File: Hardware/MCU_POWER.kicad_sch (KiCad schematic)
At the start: 28 parts, among them J4 USB_B, U1 HPM5E31IGN1, X1 24M,10ppm

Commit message: 调整引脚，拉线
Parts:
- J4: footprint Connector_USB:USB_B_OST_USB-B1HSxx_Horizontal -> Library:USB_B_OST_USB-B1HSxx_Horizontal
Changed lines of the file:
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@@
 			)
 		)
-		(property "Footprint" "Connector_USB:USB_B_OST_USB-B1HSxx_Horizontal"
+		(property "Footprint" "Library:USB_B_OST_USB-B1HSxx_Horizontal"
 			(at 146.05 172.72 0)
 			(effects
@@
 			(at 142.24 171.45 0)
 			(effects
+				(font
+					(size 1.27 1.27)
+				)
+				(hide yes)
+			)
+		)
+		(property "立创编号" ""
+			(at 142.24 171.45 0)
+			(effects
+				(font
+					(size 1.27 1.27)
+				)
+				(hide yes)
+			)
+		)
+		(property "华秋编号" ""
+			(at 142.24 171.45 0)
+			(effects

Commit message: 拉线
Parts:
- added R132, R133: 10K,1%, Resistor_SMD:R_0402_1005Metric, symbol HPM6280Foc:0402WGF1002TCE
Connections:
- net +3.3V: now also U1.M2 (DCDC_IN); no longer U1.N4 (VPMC), U1.P4 (VPMC)
- net GND: now also R132.1, R133.1; no longer U1.A1 (VSS), U1.A14 (VSS), U1.E10 (VSS), U1.E5 (VSS), U1.F7 (VSS), U1.F8 (VSS), U1.G7 (VSS), U1.G8 (VSS), U1.H7 (VSS), U1.J7 (VSS), U1.K10 (VSS), U1.K5 (VSS), U1.N3 (VSS), U1.P1 (VSS), U1.P14 (VSS)
- net RSTN: now also U1.F6 (VDD_SOC); no longer U1.M3 (RSTN)
- net USB_N: no longer U1.L13 (USB0_DN)
- net USB_P: no longer U1.L14 (USB0_DP)
- net VDD_OTPCAP: no longer U1.K8 (VDD_OTPCAP)
- net VDD_PHY0CAP: now also U1.G6 (VDD_SOC); no longer U1.J6 (VDD_PHY0CAP)
- net VDD_PMCCAP: no longer U1.K7 (VDD_PMCCAP)
- net XTALI: now also U1.M1 (DCDC_IN); no longer U1.K14 (XTALI)
- net XTALO: now also U1.N2 (DCDC_LP); no longer U1.K13 (XTALO)
- net at C22.1, R9.2: no longer U1.L12 (USB0_VBUS)
- net at U1.M1 (DCDC_IN): now also U1.M2 (DCDC_IN), R132.2
- net at U1.N2 (DCDC_LP): now also U1.P3 (DCDC_LP), R133.2
- net VDD_PHY1_CAP renamed VDD_PHY1CAP
- net VDD_PHY1CAP: no longer U1.H6 (VDD_PHY1CAP)
- no-connect marks 5 -> 1

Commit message: 修存档拉线
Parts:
- renumbered C1 to C118, C3 to C119, C4 to C120, C5 to C121, C6 to C122, C7 to C123, C8 to C124, C9 to C125, C10 to C126, C11 to C127, C12 to C128, C121 to C129, C122 to C130, C13 to C131, C14 to C132, C15 to C133, C16 to C134, C17 to C135, C18 to C136, C19 to C137, C20 to C138, C21 to C139, C22 to C140, FB1 to FB3, J4 to J22, R132 to R128, R133 to R129, R9 to R130, U1 to U3
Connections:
- net +3.3V: now also U3.N4 (VPMC), U3.P4 (VPMC); no longer U3.M2 (DCDC_IN)
- net GND: now also U3.A1 (VSS), U3.A14 (VSS), U3.E10 (VSS), U3.E5 (VSS), U3.F7 (VSS), U3.F8 (VSS), U3.G7 (VSS), U3.G8 (VSS), U3.H7 (VSS), U3.J7 (VSS), U3.K10 (VSS), U3.K5 (VSS), U3.N3 (VSS), U3.P1 (VSS), U3.P14 (VSS)
- net RSTN: now also U3.M3 (RSTN); no longer U3.F6 (VDD_SOC)
- net USB_N: now also U3.L13 (USB0_DN)
- net USB_P: now also U3.L14 (USB0_DP)
- net VDD_OTPCAP: now also U3.K8 (VDD_OTPCAP)
- net VDD_PHY0CAP: now also U3.J6 (VDD_PHY0CAP); no longer U3.G6 (VDD_SOC)
- net VDD_PHY1CAP: now also U3.H6 (VDD_PHY1CAP)
- net VDD_PMCCAP: now also U3.K7 (VDD_PMCCAP)
- net XTALI: now also U3.K14 (XTALI); no longer U3.M1 (DCDC_IN)
- net XTALO: now also U3.K13 (XTALO); no longer U3.N2 (DCDC_LP)
- net at C140.1, R130.2: now also U3.L12 (USB0_VBUS)

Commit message: 拉线
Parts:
- added C144: 100nF,16V, Capacitor_SMD:C_0402_1005Metric, symbol HPM6280Foc:CC0402KRX7R7BB104
- added R135: 10K,1%, Resistor_SMD:R_0402_1005Metric, symbol HPM6280Foc:0402WGF1002TCE
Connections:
- net +3.3V: now also R135.2
- net GND: now also C144.2
- net RSTN: now also C144.1, R135.1

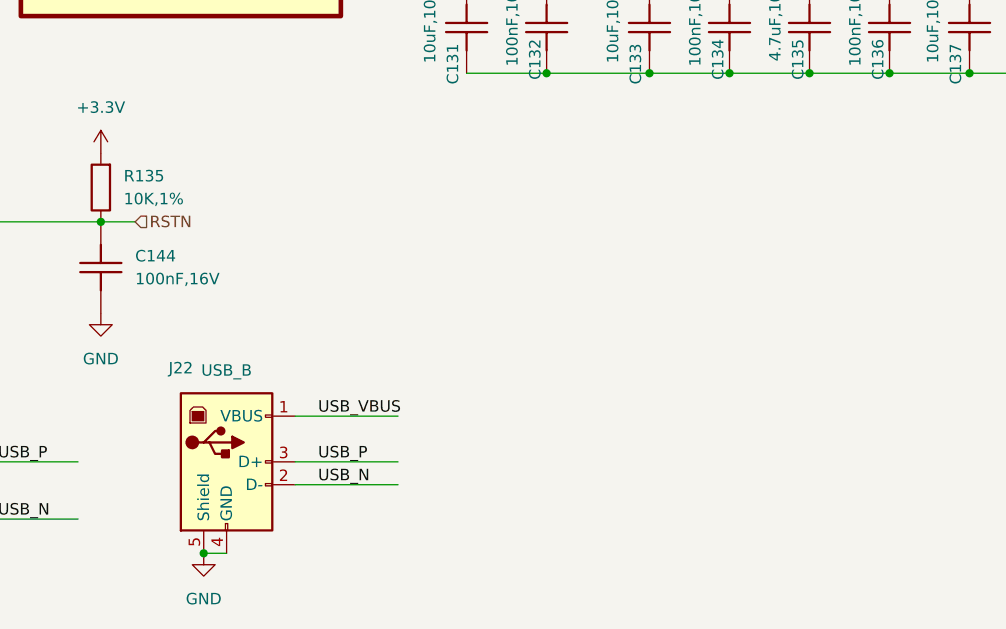
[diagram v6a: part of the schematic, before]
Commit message: 拉线，增加刹车电阻
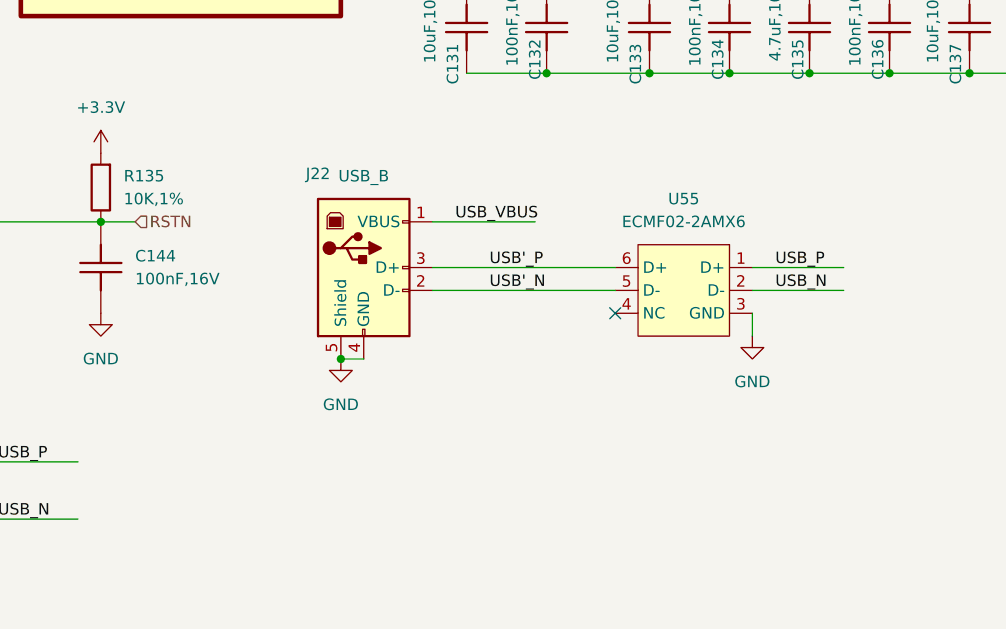
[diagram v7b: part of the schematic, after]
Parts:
- added U55: ECMF02-2AMX6, Package_DFN_QFN:ST_UQFN-6L_1.5x1.7mm_P0.5mm, symbol HPM6280Foc:ECMF02-2AMX6
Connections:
- net GND: now also U55.3 (GND)
- net USB_N: now also U55.2 (D-); no longer J22.2 (D-)
- net USB_P: now also U55.1 (D+); no longer J22.3 (D+)
- new net USB'_N: J22.2 (D-), U55.5 (D-)
- new net USB'_P: J22.3 (D+), U55.6 (D+)
- no-connect marks 1 -> 2
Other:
- moved on the sheet: J22
